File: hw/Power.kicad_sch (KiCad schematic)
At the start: 32 parts, among them J2 CONN_BAT, J3 Conn_01x05_Socket, SW1 SW_SPDT, U1 TPS3700DDCR, U2 TP4056, U3 TPS61023DRLR, U4 SPX3819M5-L-3-3, U5 TPS2111APW, U6 SPX3819M5-L-3-3

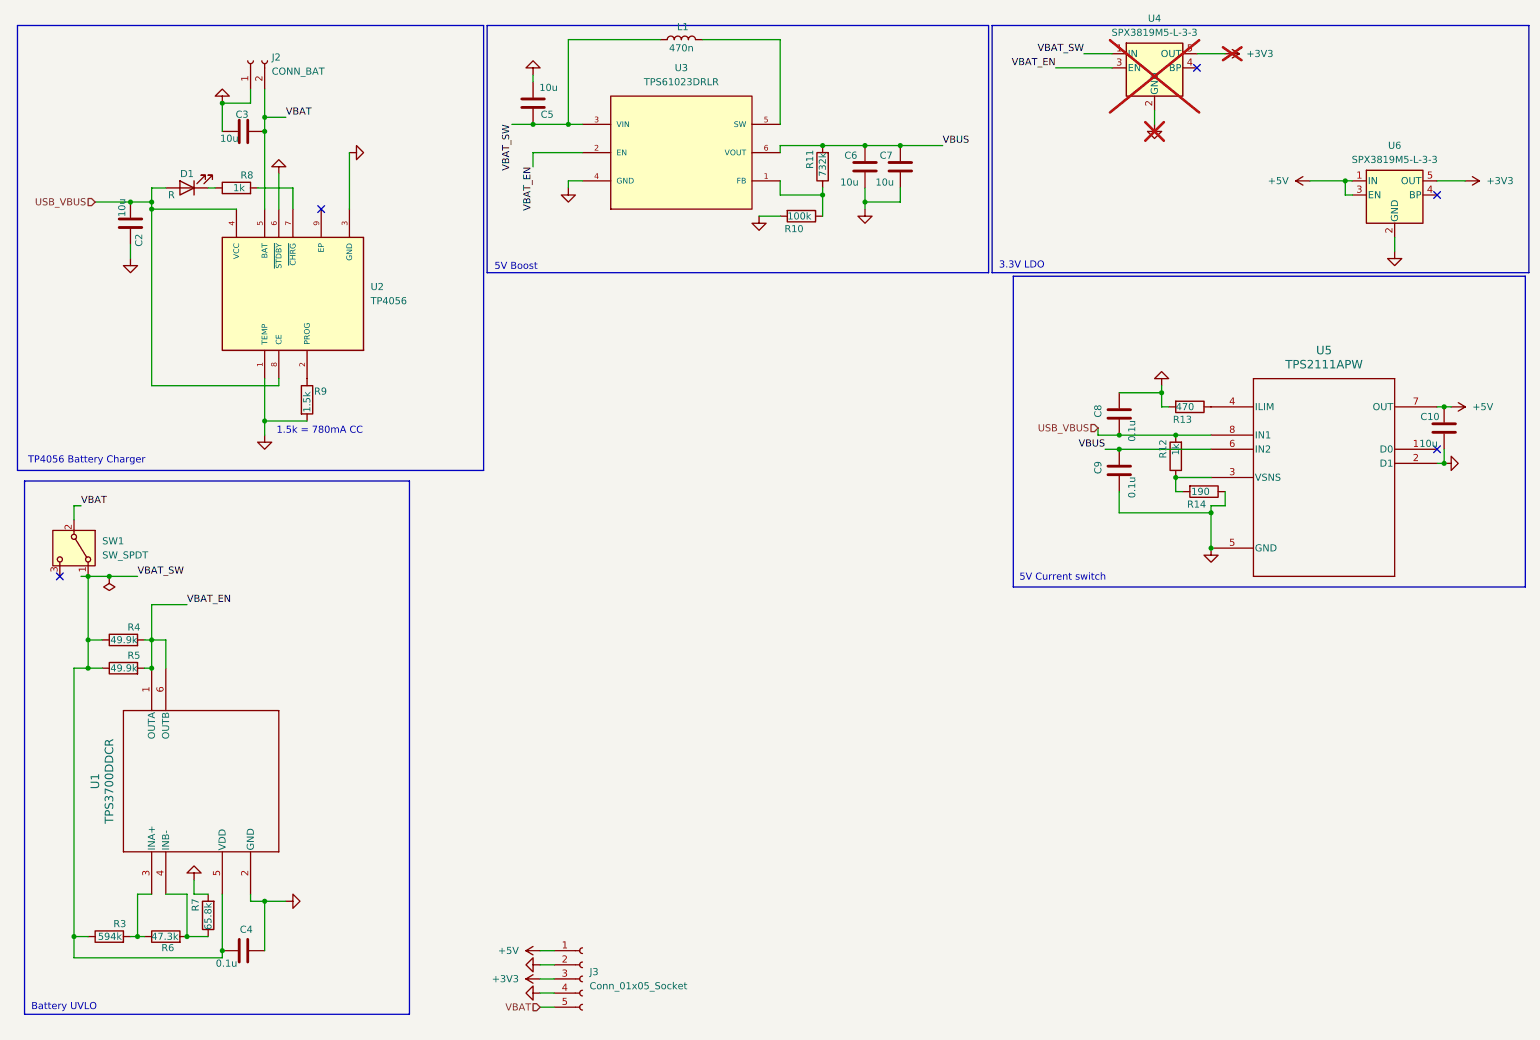
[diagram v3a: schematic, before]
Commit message: Footprinting, begin layout
I've assigned all the footprints except a few, so I've started on layout.
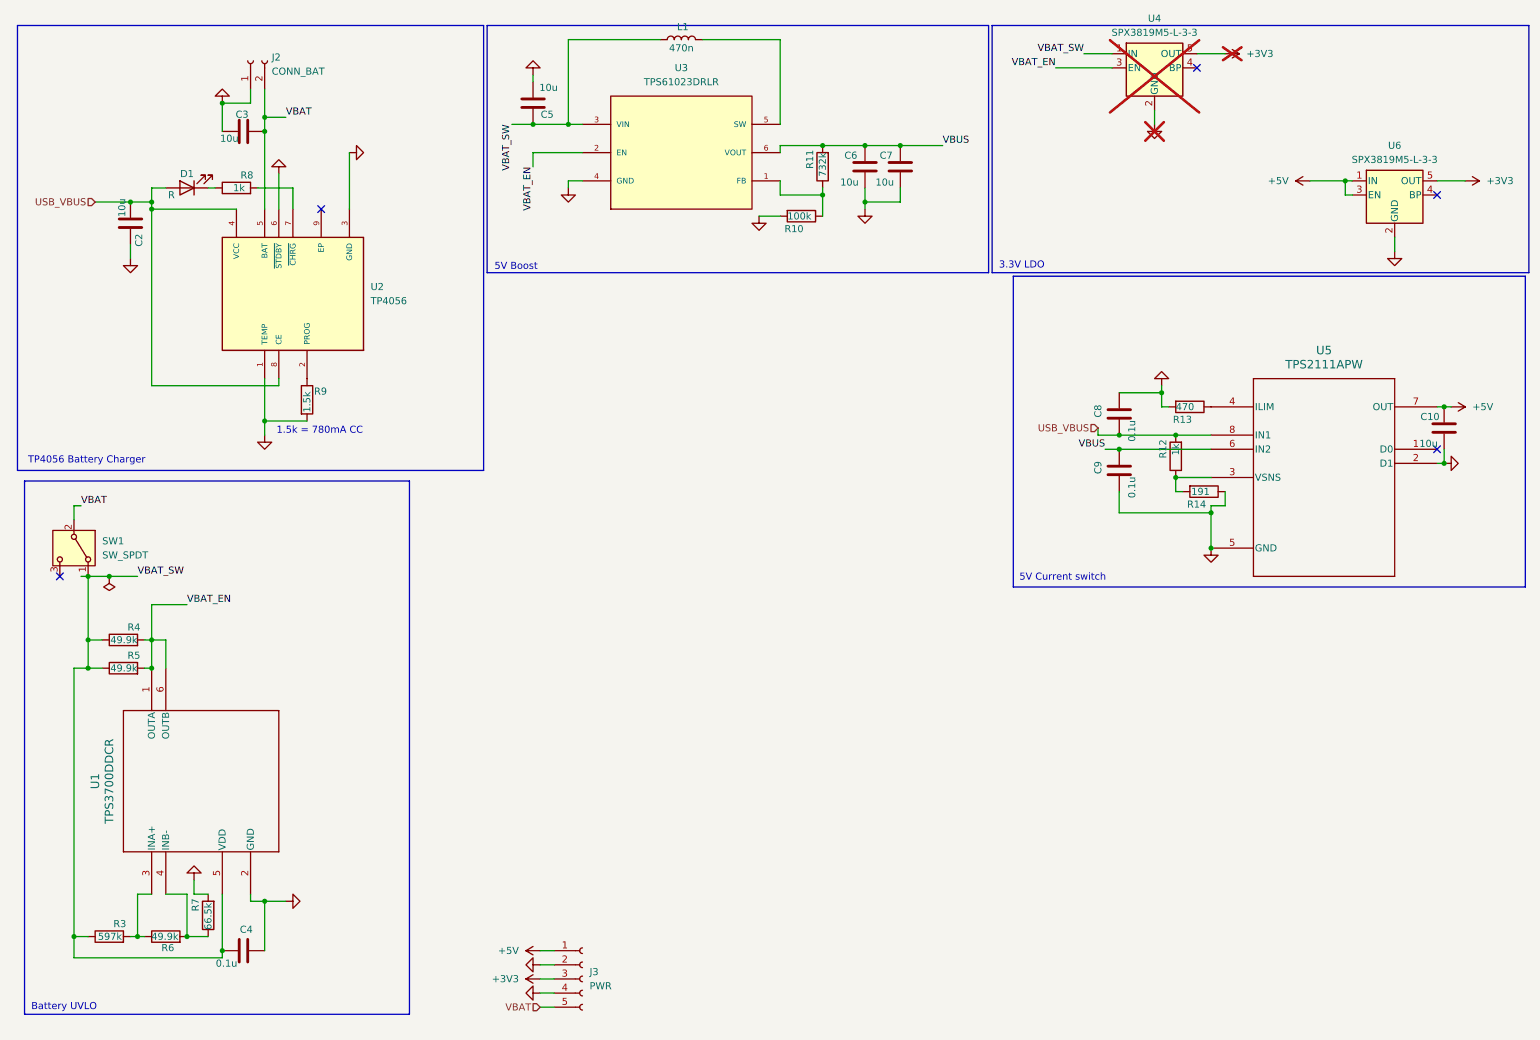
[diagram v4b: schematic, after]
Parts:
- C10: footprint Capacitor_SMD:C_0805_2012Metric_Pad1.18x1.45mm_HandSolder -> Capacitor_SMD:C_0603_1608Metric
- C2, C3, C5, C6, C7: footprint Capacitor_SMD:C_0805_2012Metric -> Capacitor_SMD:C_0603_1608Metric
- C4, C8, C9: footprint Capacitor_SMD:C_0603_1608Metric -> Capacitor_SMD:C_0402_1005Metric
- D1: footprint (none) -> LED_SMD:LED_0603_1608Metric
- J2: footprint (none) -> Connector_JST:JST_XH_B2B-XH-A_1x02_P2.50mm_Vertical
- J3: value Conn_01x05_Socket -> PWR; footprint (none) -> Connector_JST:JST_ZH_B5B-ZR_1x05_P1.50mm_Vertical
- R10, R11, R12, R13, R4, R5, R8, R9: footprint (none) -> Resistor_SMD:R_0603_1608Metric
- R14: value 190 -> 191; footprint (none) -> Resistor_SMD:R_0603_1608Metric
- R3: value 594k -> 597k; footprint (none) -> Resistor_SMD:R_0603_1608Metric
- R6: value 47.3k -> 49.9k; footprint (none) -> Resistor_SMD:R_0603_1608Metric
- R7: value 65.8k -> 66.5k; footprint (none) -> Resistor_SMD:R_0603_1608Metric
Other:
- title: (none) -> Weltkatze
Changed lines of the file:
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@@
 	(generator_version "8.0")
 	(paper "A4")
+	(title_block
+		(title "Weltkatze")
+		(date "2025-02-25")
+		(rev "1")
+	)
 	(junction
 		(at 165.1 44.45)
@@
 			)
 		)
-		(property "Footprint" "Capacitor_SMD:C_0603_1608Metric"
+		(property "Footprint" "Capacitor_SMD:C_0402_1005Metric"
 			(at 57.15 178.1048 0)
 			(effects
@@
 			)
 		)
-		(property "Footprint" "Capacitor_SMD:C_0603_1608Metric"
+		(property "Footprint" "Capacitor_SMD:C_0402_1005Metric"
 			(at 209.8548 88.9 0)
 			(effects
@@
 			)
 		)
-		(property "Footprint" "Capacitor_SMD:C_0805_2012Metric"
+		(property "Footprint" "Capacitor_SMD:C_0603_1608Metric"
 			(at 172.4152 41.91 0)
 			(effects
@@
 			)
 		)
-		(property "Value" "65.8k"
+		(property "Value" "66.5k"
 			(at 46.99 170.434 90)
 			(effects
@@
 			)
 		)
-		(property "Footprint" ""
+		(property "Footprint" "Resistor_SMD:R_0603_1608Metric"
 			(at 48.768 172.72 90)
 			(effects
@@
 			)
 		)
-		(property "Footprint" ""
+		(property "Footprint" "Resistor_SMD:R_0603_1608Metric"
 			(at 153.67 45.212 90)
 			(effects
@@
 			)
 		)
-		(property "Footprint" "Capacitor_SMD:C_0805_2012Metric"
+		(property "Footprint" "Capacitor_SMD:C_0603_1608Metric"
 			(at 104.4448 22.86 0)
 			(effects
@@
 			)
 		)
-		(property "Footprint" ""
+		(property "Footprint" "Resistor_SMD:R_0603_1608Metric"
 			(at 222.758 90.17 90)
 			(effects
@@
 			)
 		)
-		(property "Footprint" ""
+		(property "Footprint" "Resistor_SMD:R_0603_1608Metric"
 			(at 31.75 124.968 90)
 			(effects
@@
 			)
 		)
-		(property "Footprint" "Capacitor_SMD:C_0805_2012Metric"
+		(property "Footprint" "Capacitor_SMD:C_0603_1608Metric"
 			(at 49.53 32.7152 0)
 			(effects
@@
 			)
 		)
-		(property "Footprint" ""
+		(property "Footprint" "LED_SMD:LED_0603_1608Metric"
 			(at 43.18 41.91 0)
 			(effects
@@
 			)
 		)
-		(property "Footprint" "Capacitor_SMD:C_0805_2012Metric"
+		(property "Footprint" "Capacitor_SMD:C_0603_1608Metric"
 			(at 33.9852 52.07 0)
 			(effects
@@
 			)
 		)
-		(property "Footprint" ""
+		(property "Footprint" "Resistor_SMD:R_0603_1608Metric"
 			(at 159.258 38.1 90)
 			(effects
@@
 			)
 		)
-		(property "Value" "594k"
+		(property "Value" "597k"
 			(at 31.496 176.53 90)
 			(effects
@@
 			)
 		)
-		(property "Footprint" ""
+		(property "Footprint" "Resistor_SMD:R_0603_1608Metric"
 			(at 29.21 178.308 90)
 			(effects
@@
 			)
 		)
-		(property "Footprint" ""
+		(property "Footprint" "Resistor_SMD:R_0603_1608Metric"
 			(at 31.75 130.048 90)
 			(effects
@@
 			)
 		)
-		(property "Footprint" ""
+		(property "Footprint" "Resistor_SMD:R_0603_1608Metric"
 			(at 223.52 79.502 90)
 			(effects
@@
 			)
 		)
-		(property "Footprint" ""
+		(property "Footprint" "Resistor_SMD:R_0603_1608Metric"
 			(at 52.07 43.688 90)
 			(effects
@@
 			)
 		)
-		(property "Value" "47.3k"
+		(property "Value" "49.9k"
 			(at 41.656 176.53 90)
 			(effects
@@
 			)
 		)
-		(property "Footprint" ""
+		(property "Footprint" "Resistor_SMD:R_0603_1608Metric"
 			(at 39.37 178.308 90)
 			(effects
@@
 			)
 		)
-		(property "Footprint" "Capacitor_SMD:C_0603_1608Metric"
+		(property "Footprint" "Capacitor_SMD:C_0402_1005Metric"
 			(at 209.8548 78.74 0)
 			(effects
@@
 			)
 		)
-		(property "Footprint" ""
+		(property "Footprint" "Resistor_SMD:R_0603_1608Metric"
 			(at 62.992 80.01 90)
 			(effects
@@
 			)
 		)
-		(property "Footprint" "Capacitor_SMD:C_0805_2012Metric"
+		(property "Footprint" "Capacitor_SMD:C_0603_1608Metric"
 			(at 166.0652 41.91 0)
 			(effects
@@
 			)
 		)
-		(property "Footprint" ""
+		(property "Footprint" "Connector_JST:JST_XH_B2B-XH-A_1x02_P2.50mm_Vertical"
 			(at 54.61 19.05 0)
 			(effects
@@
 			)
 		)
-		(property "Footprint" "Capacitor_SMD:C_0805_2012Metric_Pad1.18x1.45mm_HandSolder"
+		(property "Footprint" "Capacitor_SMD:C_0603_1608Metric"
 			(at 270.2052 88.9 0)
 			(effects
@@
 			)
 		)
-		(property "Value" "Conn_01x05_Socket"
+		(property "Value" "PWR"
 			(at 115.57 185.4199 0)
 			(effects
@@
 			)
 		)
-		(property "Footprint" ""
+		(property "Footprint" "Connector_JST:JST_ZH_B5B-ZR_1x05_P1.50mm_Vertical"
 			(at 114.3 184.15 0)
 			(effects
@@
 			)
 		)
-		(property "Value" "190"
+		(property "Value" "191"
 			(at 223.774 96.52 90)
 			(effects
@@
 			)
 		)
-		(property "Footprint" ""
+		(property "Footprint" "Resistor_SMD:R_0603_1608Metric"
 			(at 226.06 94.742 90)
 			(effects

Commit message: yes
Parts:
- U2: footprint TP4056:SOP127P600X175-9N -> lib:SOP127P600X175-9N
- U3: footprint TPS61023DRLR:DRL0006A -> lib:DRL0006A
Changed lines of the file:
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@@
 			)
 		)
-		(property "Footprint" "TPS61023DRLR:DRL0006A"
+		(property "Footprint" "lib:DRL0006A"
 			(at 132.08 35.56 0)
 			(effects
@@
 			)
 		)
-		(property "Footprint" "TP4056:SOP127P600X175-9N"
+		(property "Footprint" "lib:SOP127P600X175-9N"
 			(at 62.23 60.96 0)
 			(effects

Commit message: Rest of the owl
Finish major layout, minor tweaks can be made
E.g. rotating the LEDs so they look pretty

Still need to make it so the inner PCB is manufacturable
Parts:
- removed U4: SPX3819M5-L-3-3, Package_TO_SOT_SMD:SOT-23-5, symbol Regulator_Linear:SPX3819M5-L-3-3
- J3: footprint Connector_JST:JST_ZH_B5B-ZR_1x05_P1.50mm_Vertical -> Connector_JST:JST_ZH_B6B-ZR_1x06_P1.50mm_Vertical; symbol Connector:Conn_01x05_Socket -> Connector:Conn_01x06_Socket
- L1: footprint (none) -> Inductor_SMD:L_0805_2012Metric
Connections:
- net +3V3: no longer J3.3 (Pin_3)
- net +5V: now also J3.4 (Pin_4); no longer J3.1 (Pin_1)
- net GND: now also J3.3 (Pin_3), J3.5 (Pin_5), U2.9 (EP); no longer J3.2 (Pin_2), J3.4 (Pin_4)
- net VBAT: now also SW1.3 (C); no longer J3.5 (Pin_5), SW1.2 (B)
- net VBAT_SW: now also SW1.2 (B); no longer SW1.1 (A)
- new net USBD_N: J3.2 (Pin_2)
- new net USBD_P: J3.1 (Pin_1)
- new net VBAT_MON: J3.6 (Pin_6)
- no-connect marks 5 -> 3
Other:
- moved on the sheet: SW1

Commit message: V1 REV1 Final!
I consider this design finished, as such I've submitted it to JLCPCB

I converted to a 6L pcb because its cheaper, in.3 and in.4 have no copper
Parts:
- removed SW1: SW_SPDT, Button_Switch_THT:SW_Slide_SPDT_Straight_CK_OS102011MS2Q, symbol Switch:SW_SPDT
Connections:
- net VBAT_SW is gone; now on net VBAT: C4.1, C5.1, L1.1, R3.1, R4.1, R5.1, U1.5 (VDD), U3.3 (VIN)
- net USBD_N: no longer names the net of J3.2 (Pin_2)
- net USBD_P: no longer names the net of J3.1 (Pin_1)
- no-connect marks 3 -> 2

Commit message: Minor reroute
Minor reroute of traces, utilises all 6 layers effectively now.
Also reduces some issues with USB going through multiple layers unnecessarily
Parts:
- J3: now not fitted
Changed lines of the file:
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@@
 		(exclude_from_sim no)
 		(in_bom yes)
-		(on_board yes)
-		(dnp no)
+		(on_board no)
+		(dnp yes)
 		(fields_autoplaced yes)
 		(property "Reference" "J3"
